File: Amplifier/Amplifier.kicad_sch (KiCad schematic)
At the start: 39 parts, among them J1 Screw_Terminal_01x02, J3 Screw_Terminal_01x02, U1 PA88

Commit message: update
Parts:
- added JP1: Jumper_2_Open, Jumper:SolderJumper-2_P1.3mm_Open_RoundedPad1.0x1.5mm, symbol Jumper:Jumper_2_Open
- added R14, R15: 68k, Resistor_SMD:R_1206_3216Metric_Pad1.30x1.75mm_HandSolder, symbol Device:R_Small_US
- added R7: 100, Resistor_SMD:R_1206_3216Metric_Pad1.30x1.75mm_HandSolder, symbol Device:R_Small_US
- R11, R12, R8: value 110K -> 68k
- R6: value 100 -> 11
- R9: value 110K -> 68K
- RV1: value 200 -> 100
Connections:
- net +VHV: now also R15.2; no longer R8.2
- net GND: now also H3.1, JP1.1 (A), R7.2; no longer H4.1, R2.2
- net at R11.1: now also R14.2; no longer R12.2
- new net: R15.1, R8.2
- new net: JP1.2 (B), R2.2, R7.1
- new net: R12.2, R14.1
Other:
- moved on the sheet: H3, R11, R2

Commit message: update
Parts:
- removed JP1: Jumper_2_Open, Jumper:SolderJumper-2_P1.3mm_Open_RoundedPad1.0x1.5mm, symbol Jumper:Jumper_2_Open
- R3: value 10M -> 330k
- R4, R5: value 49.9K -> 50K; Part Description 2019-RN73H2BTTD2003A05CT-ND -> (none)
- R7: value 100 -> 160
- RV1: value 100 -> 10
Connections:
- net GND: now also H1.1
- net at R2.2, R7.1: now also R3.1
- net at R2.1, RV1.2, RV1.3: no longer R3.1
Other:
- moved on the sheet: R10, R13, R3, RV2

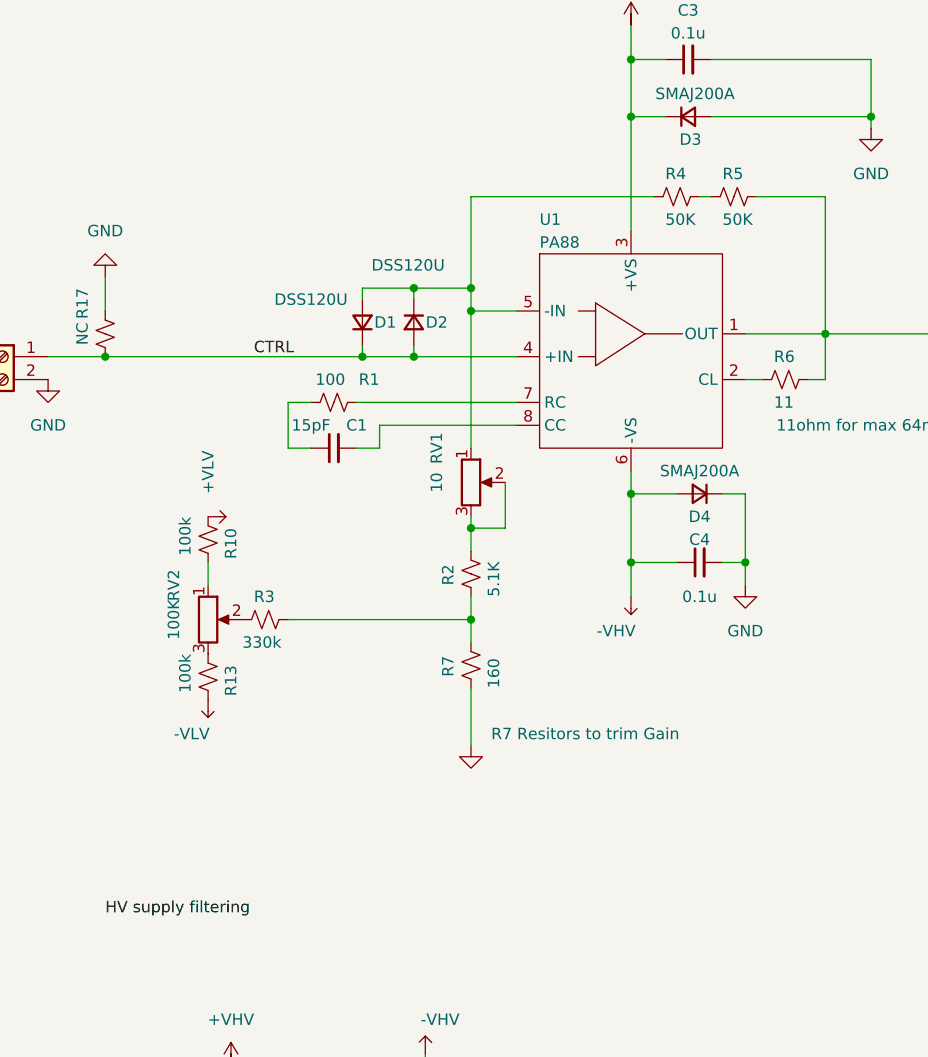
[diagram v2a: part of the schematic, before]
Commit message: update feedback resistor to 200k
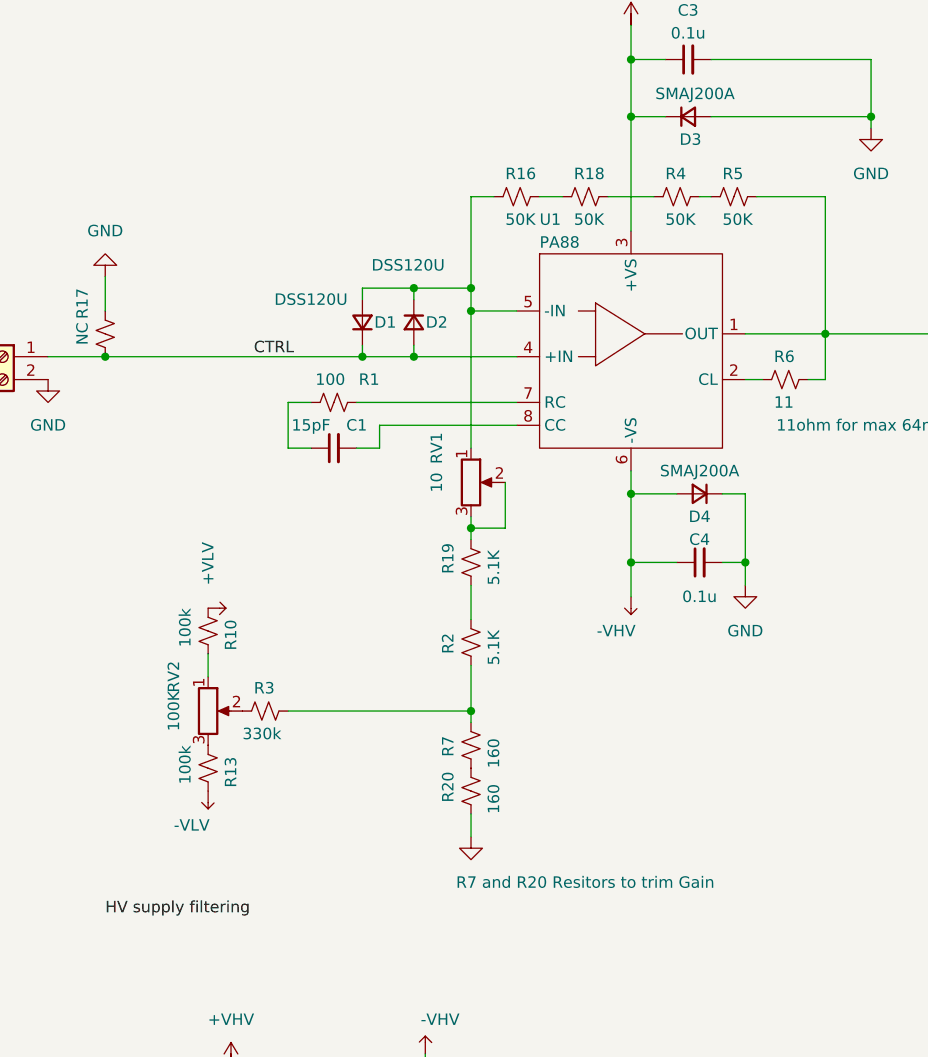
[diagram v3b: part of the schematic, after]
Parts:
- added R16, R18: 50K, Resistor_SMD:R_1206_3216Metric_Pad1.30x1.75mm_HandSolder, symbol Device:R_Small_US
- added R19: 5.1K, Resistor_SMD:R_1206_3216Metric_Pad1.30x1.75mm_HandSolder, symbol Device:R_Small_US
- added R20: 160, Resistor_SMD:R_1206_3216Metric_Pad1.30x1.75mm_HandSolder, symbol Device:R_Small_US
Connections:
- net GND: now also R20.2; no longer R7.2
- net at D1.2 (A), D2.1 (K), RV1.1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: now also R16.2; no longer R4.2
- net at RV1.2, RV1.3: now also R19.1; no longer R2.1
- new net: R18.1, R4.2
- new net: R20.1, R7.2
- new net: R16.1, R18.2
- new net: R19.2, R2.1
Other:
- moved on the sheet: R10, R13, R2, R3, R7, RV2
